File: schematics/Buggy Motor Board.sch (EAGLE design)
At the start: 42 parts, among them CON0 M025MM, CON1 M025MM, X1 MICROSD, X2 5566-24, X3 5566-24

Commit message: Tweak for Master
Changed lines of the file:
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@@
 <instance part="R11" gate="G$1" x="228.6" y="259.08" rot="MR0"/>
 <instance part="GND7" gate="1" x="248.92" y="241.3"/>
-<instance part="X1" gate="G$1" x="71.12" y="170.18"/>
-<instance part="+3V2" gate="G$1" x="48.26" y="165.1"/>
-<instance part="SUPPLY2" gate="GND" x="53.34" y="144.78"/>
+<instance part="X1" gate="G$1" x="71.12" y="172.72"/>
+<instance part="+3V2" gate="G$1" x="48.26" y="167.64"/>
+<instance part="SUPPLY2" gate="GND" x="53.34" y="147.32"/>
 <instance part="U$8" gate="G$1" x="96.52" y="60.96" rot="MR0"/>
 <instance part="GND9" gate="1" x="66.04" y="30.48"/>
@@
 </segment>
 <segment>
-<wire x1="53.34" y1="157.48" x2="53.34" y2="152.4" width="0.1524" layer="91"/>
+<wire x1="53.34" y1="160.02" x2="53.34" y2="154.94" width="0.1524" layer="91"/>
+<wire x1="53.34" y1="154.94" x2="53.34" y2="152.4" width="0.1524" layer="91"/>
 <wire x1="53.34" y1="152.4" x2="53.34" y2="149.86" width="0.1524" layer="91"/>
-<wire x1="53.34" y1="149.86" x2="53.34" y2="147.32" width="0.1524" layer="91"/>
+<junction x="53.34" y="154.94"/>
 <junction x="53.34" y="152.4"/>
-<junction x="53.34" y="149.86"/>
 <pinref part="X1" gate="G$1" pin="VSS"/>
 <pinref part="X1" gate="G$1" pin="GND1"/>
@@
 <net name="MISO" class="0">
 <segment>
-<wire x1="40.64" y1="177.8" x2="53.34" y2="177.8" width="0.1524" layer="91"/>
-<label x="40.64" y="177.8" size="1.778" layer="95"/>
+<wire x1="40.64" y1="180.34" x2="53.34" y2="180.34" width="0.1524" layer="91"/>
+<label x="40.64" y="180.34" size="1.778" layer="95"/>
 <pinref part="X1" gate="G$1" pin="DATA_OUT"/>
 </segment>
@@
 </segment>
 <segment>
-<wire x1="40.64" y1="175.26" x2="53.34" y2="175.26" width="0.1524" layer="91"/>
+<wire x1="40.64" y1="177.8" x2="53.34" y2="177.8" width="0.1524" layer="91"/>
 <pinref part="X1" gate="G$1" pin="DATA_IN"/>
-<label x="40.64" y="175.26" size="1.778" layer="95"/>
+<label x="40.64" y="177.8" size="1.778" layer="95"/>
 </segment>
 </net>
@@
 <net name="+3V3" class="0">
 <segment>
-<wire x1="48.26" y1="162.56" x2="48.26" y2="160.02" width="0.1524" layer="91"/>
-<wire x1="48.26" y1="160.02" x2="53.34" y2="160.02" width="0.1524" layer="91"/>
+<wire x1="48.26" y1="165.1" x2="48.26" y2="162.56" width="0.1524" layer="91"/>
+<wire x1="48.26" y1="162.56" x2="53.34" y2="162.56" width="0.1524" layer="91"/>
 <pinref part="X1" gate="G$1" pin="VDD"/>
 <pinref part="+3V2" gate="G$1" pin="+3V3"/>
@@
 <net name="CD" class="0">
 <segment>
-<wire x1="53.34" y1="187.96" x2="40.64" y2="187.96" width="0.1524" layer="91"/>
-<label x="40.64" y="187.96" size="1.778" layer="95"/>
+<wire x1="53.34" y1="190.5" x2="40.64" y2="190.5" width="0.1524" layer="91"/>
+<label x="40.64" y="190.5" size="1.778" layer="95"/>
 <pinref part="X1" gate="G$1" pin="CARD_DETECT"/>
 </segment>
@@
 </segment>
 <segment>
-<wire x1="40.64" y1="170.18" x2="53.34" y2="170.18" width="0.1524" layer="91"/>
+<wire x1="40.64" y1="172.72" x2="53.34" y2="172.72" width="0.1524" layer="91"/>
 <pinref part="X1" gate="G$1" pin="CS"/>
-<label x="40.64" y="170.18" size="1.778" layer="95"/>
+<label x="40.64" y="172.72" size="1.778" layer="95"/>
 </segment>
 </net>
@@
 </segment>
 <segment>
-<wire x1="40.64" y1="172.72" x2="53.34" y2="172.72" width="0.1524" layer="91"/>
+<wire x1="40.64" y1="175.26" x2="53.34" y2="175.26" width="0.1524" layer="91"/>
 <pinref part="X1" gate="G$1" pin="SCLK"/>
-<label x="40.64" y="172.72" size="1.778" layer="95"/>
-</segment>
-</net>
+<label x="40.64" y="175.26" size="1.778" layer="95"/>
+</segment>
+</net>

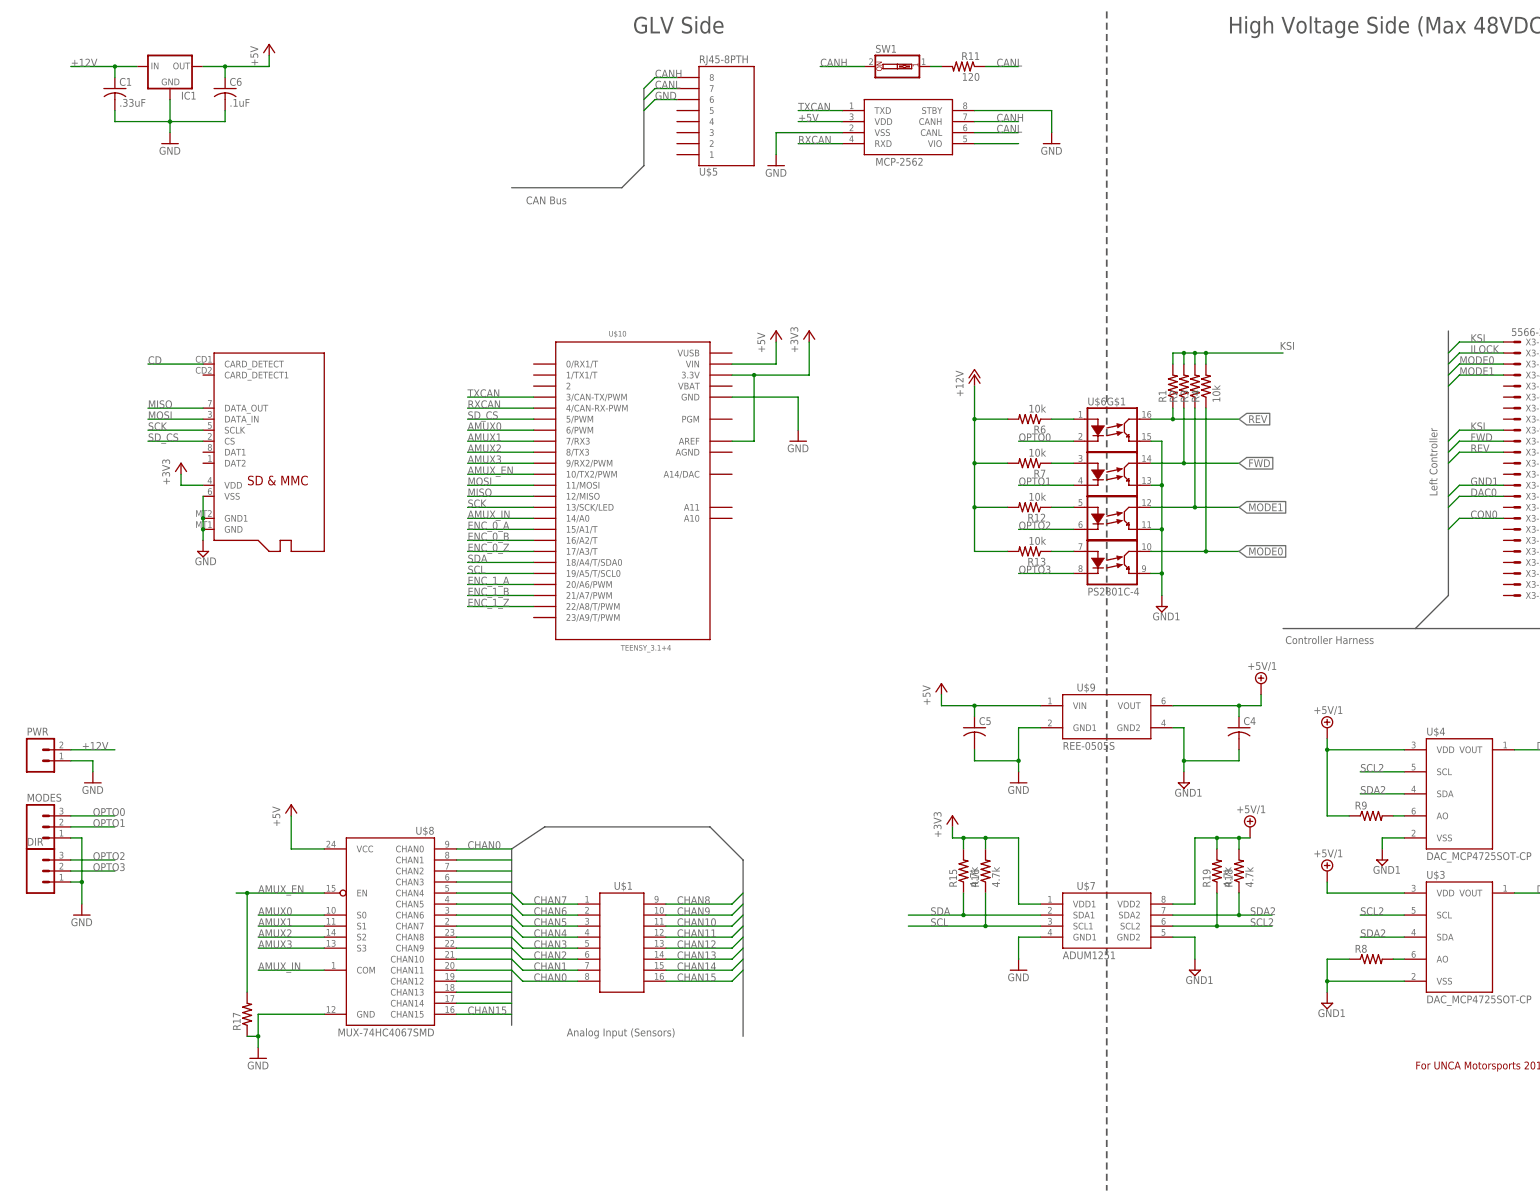
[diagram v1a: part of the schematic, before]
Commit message: Add Quadrature Counter, RTC, MPU, CAN Bus 2
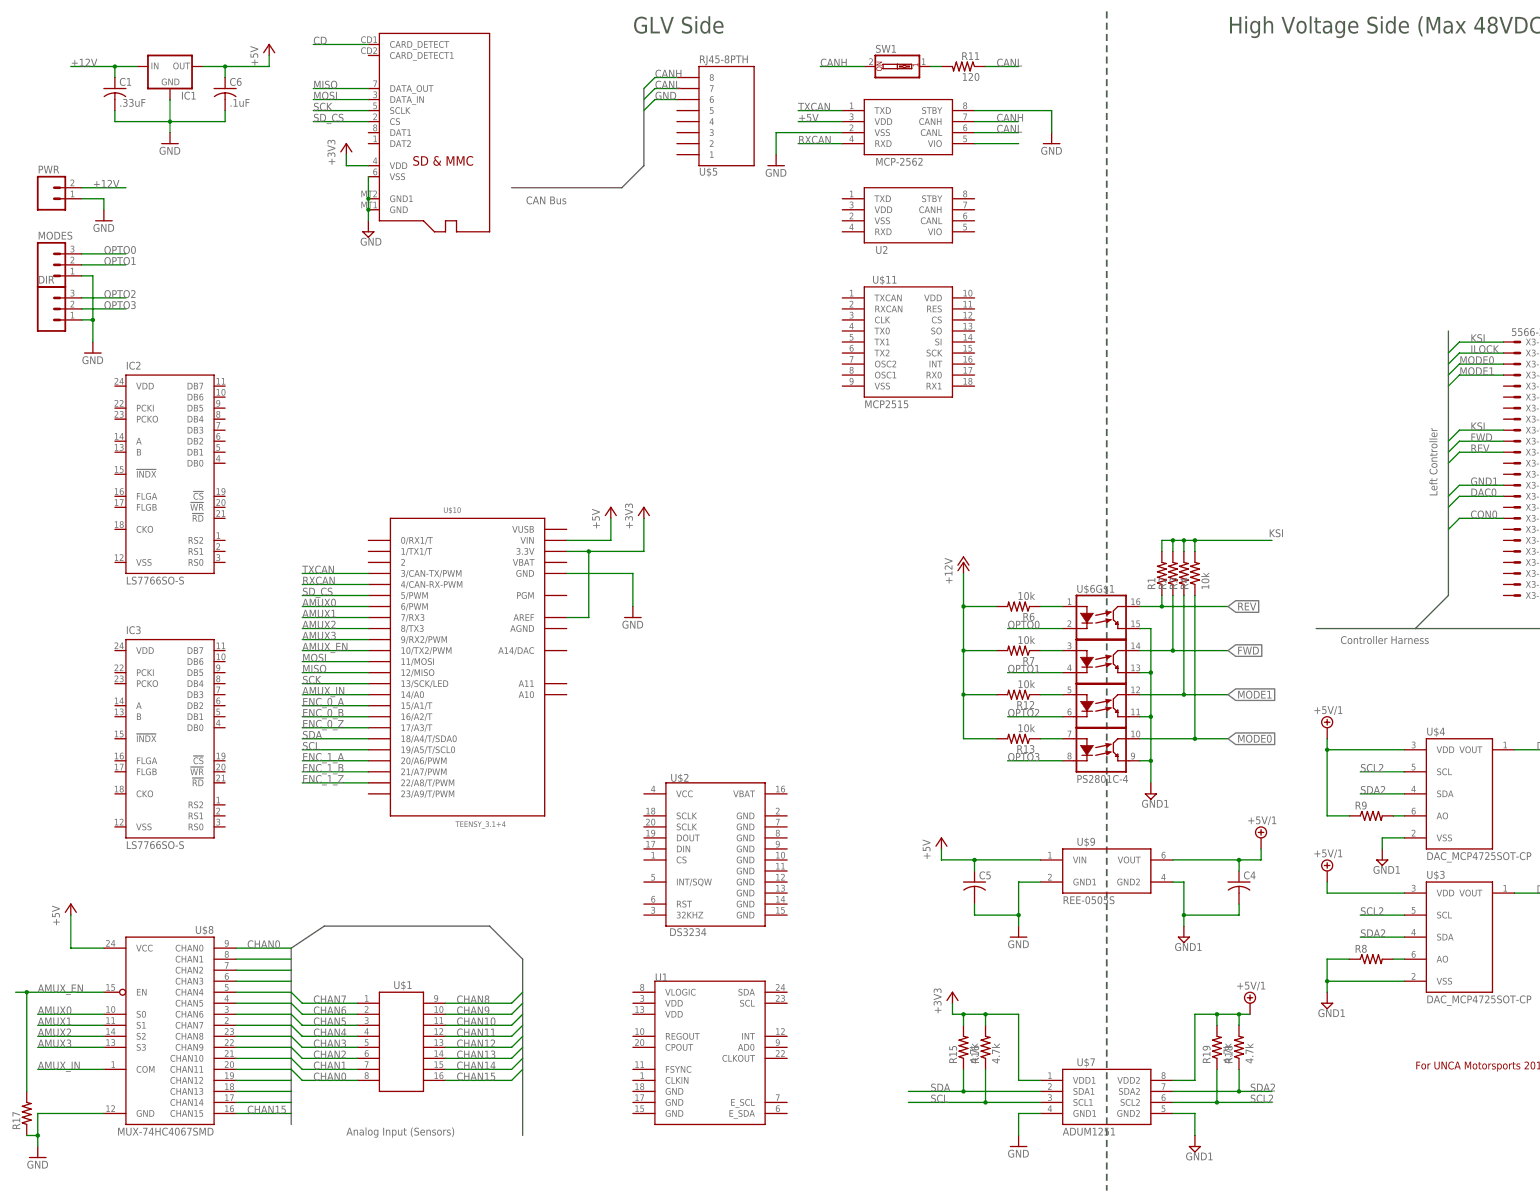
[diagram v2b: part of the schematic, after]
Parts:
- added IC2, IC3: LS7766SO-S, lsi-computer-systems:LS7766SO-S
- added U$11: MCP2515, Wetmelon-DigitalIC:MCP2515
- added U$2: DS3234, SparkFun-FreqCtrl:DS3234
- added U1: (no value), SparkFun-Sensors:MPU-9150QFN-24-NP
- added U2: MCP2562, Wetmelon-DigitalIC:MCP2562
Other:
- moved on the sheet: C4, C5, DIR, MODES, PWR, R1, R12, R13, R15, R16, R17, R18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

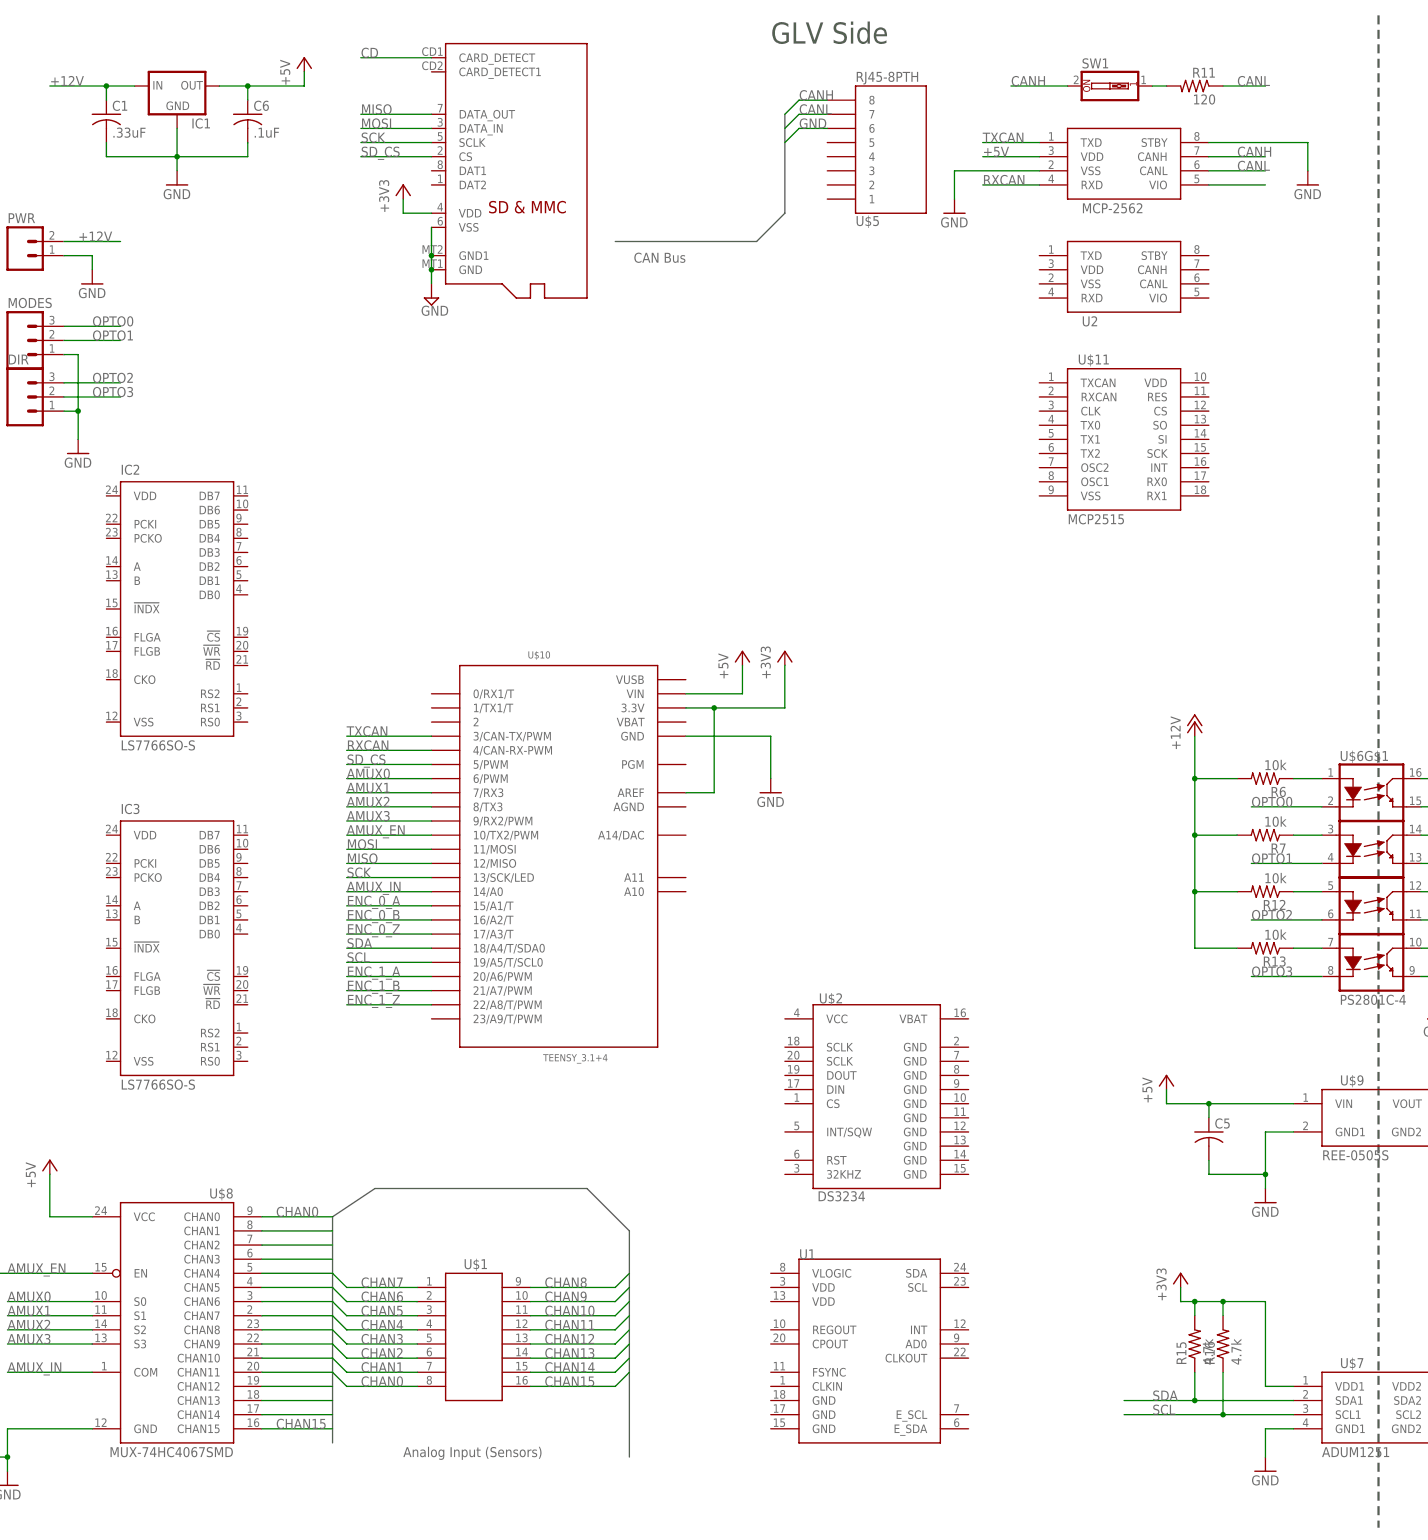
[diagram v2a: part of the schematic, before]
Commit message: Schematic changes
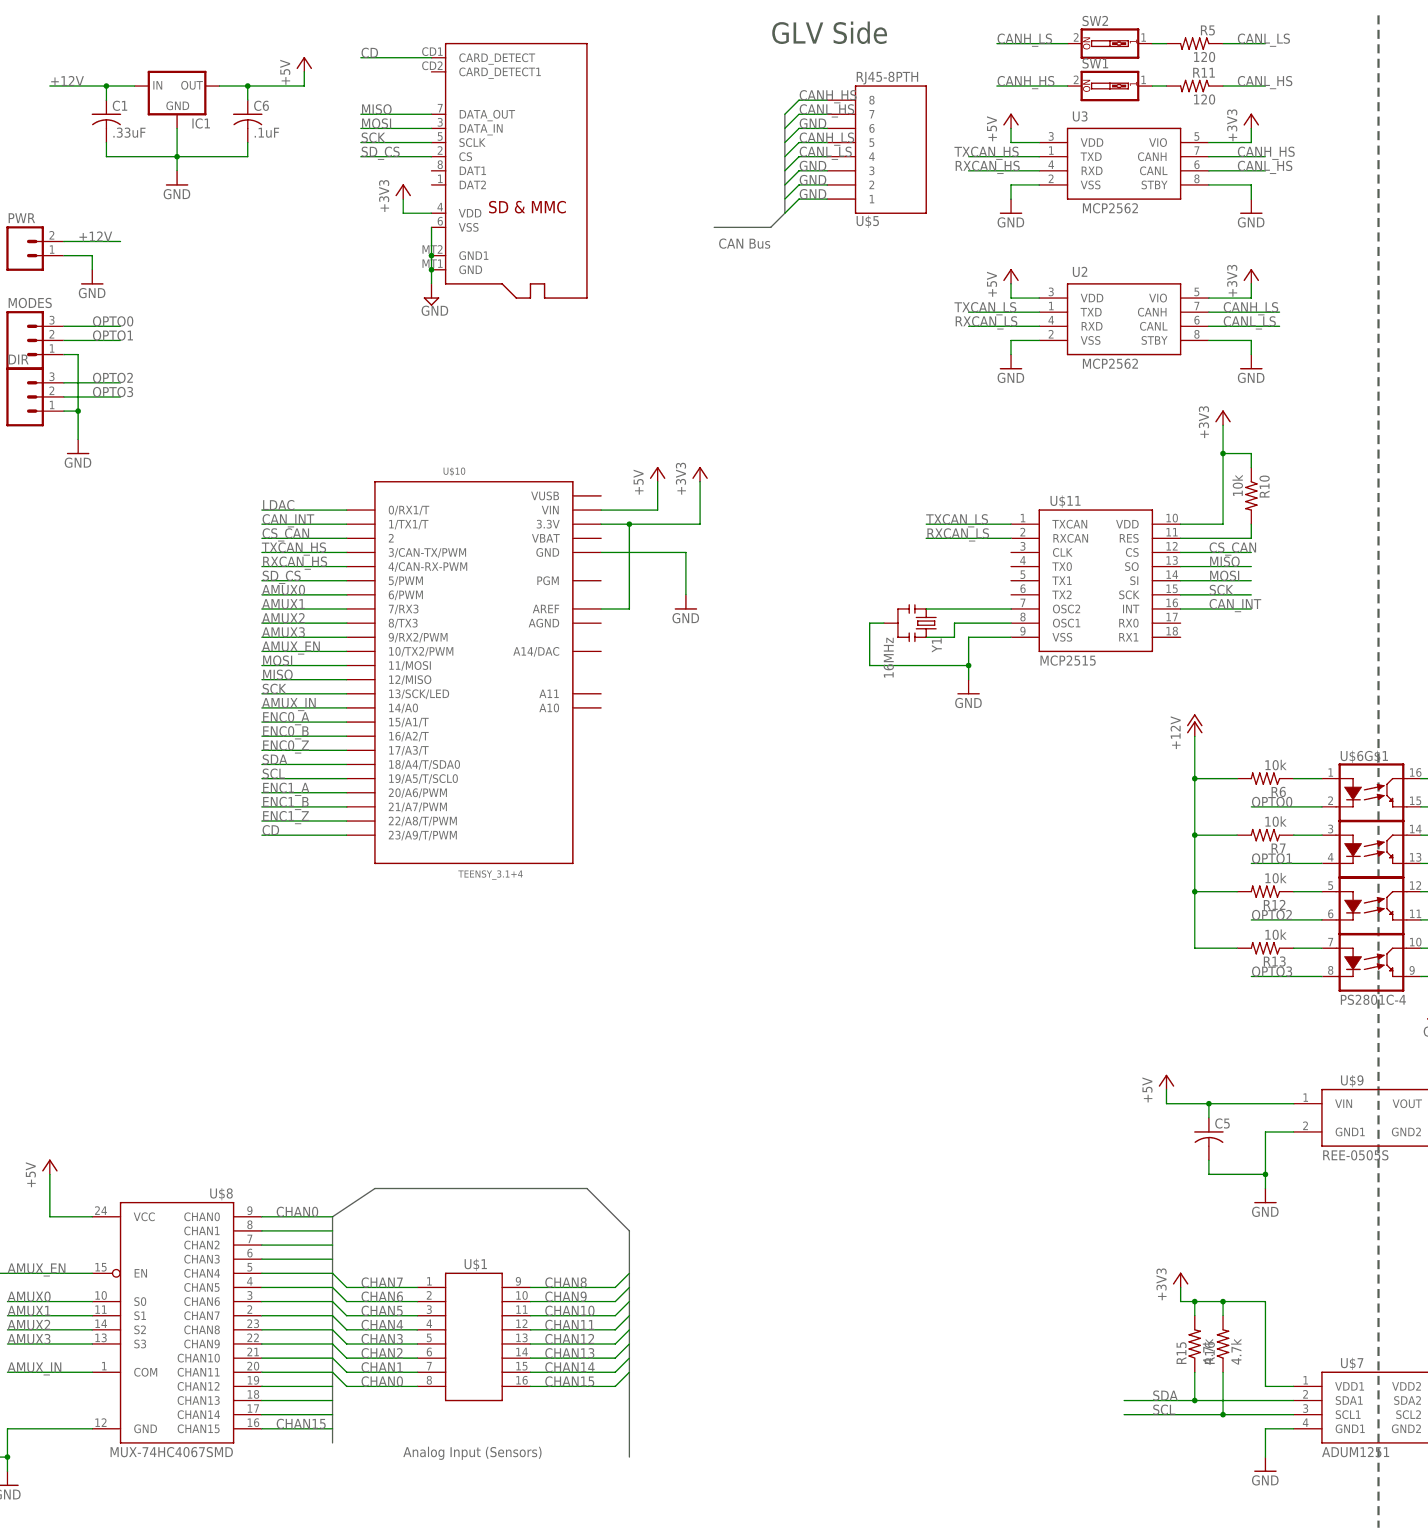
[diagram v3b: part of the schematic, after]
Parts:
- removed IC2, IC3: LS7766SO-S, lsi-computer-systems:LS7766SO-S
- removed U$2: DS3234, SparkFun-FreqCtrl:DS3234
- removed U1: (no value), SparkFun-Sensors:MPU-9150QFN-24-NP
- added R10: 10k, SparkFun-Resistors:RESISTOR0805-RES
- added R5: 120, SparkFun-Resistors:RESISTOR0805-RES
- added SW2: (no value), special:SW_DIP-1
- added Y1: 16MHz, SparkFun-FreqCtrl:RESONATORPTH
- renumbered MCP-2562 to U3
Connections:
- net CANH renamed CANH_HS
- net CANL renamed CANL_HS
- net ENC_0_A renamed ENC0_A
- net ENC_0_B renamed ENC0_B
- net ENC_0_Z renamed ENC0_Z
- net ENC_1_A renamed ENC1_A
- net ENC_1_B renamed ENC1_B
- net ENC_1_Z renamed ENC1_Z
- net RXCAN renamed RXCAN_HS
- net TXCAN renamed TXCAN_HS
- new net CANH_LS: SW2.2, U$5.5, U2.CANH
- new net CANL_LS: R5.1, U$5.4, U2.CANL
- new net CAN_INT: U$10.1/TX1/T, U$11.INT
- new net CS_CAN: U$10.2, U$11.CS
- new net LDAC: U$10.0/RX1/T
- new net N$1: R5.2, SW2.1
- new net N$10: U$11.OSC1, Y1.3
- new net N$14: R10.2, U$11.RES
- new net N$9: U$11.OSC2, Y1.1
- new net RXCAN_LS: U$11.RXCAN, U2.RXD
- new net TXCAN_LS: U$11.TXCAN, U2.TXD
- net +3V3: now also R10.1, U$11.VDD, U2.VIO
- net +5V: now also U2.VDD
- net CD: now also U$10.23/A9/T/PWM
- net GND: now also U$11.VSS, U$5.1, U$5.2, U$5.3, U2.STBY, U2.VSS, Y1.2
- net MISO: now also U$11.SO
- net MOSI: now also U$11.SI
- net SCK: now also U$11.SCK
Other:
- moved on the sheet: U$10, U$11, U2
